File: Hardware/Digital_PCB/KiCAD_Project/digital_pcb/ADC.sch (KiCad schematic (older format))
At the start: 16 parts, among them U4 ADS1220, U5 KC2520B-C2

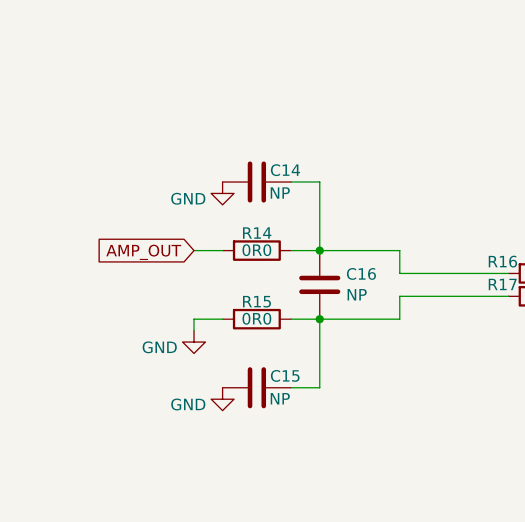
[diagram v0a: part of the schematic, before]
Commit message: Add pullups and divider for ADC input.
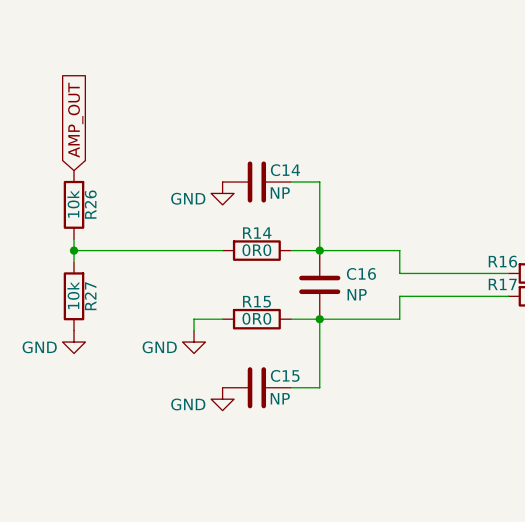
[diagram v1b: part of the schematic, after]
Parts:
- added R26, R27: 10k, Resistors_SMD:R_0603_HandSoldering, symbol Device:R
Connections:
- net AMP_OUT: now also R26.2; no longer R14.2
- net GND: now also R27.1
- new net: R14.2, R26.1, R27.2
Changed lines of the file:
@@
 Wire Wire Line
 	6150 3500 6150 3375
-Text GLabel 3525 2575 0    50   Input ~ 0
-AMP_OUT
-Wire Wire Line
-	3525 2575 3650 2575
 $Comp
 L power:GND #PWR032
@@
 NoConn ~ 5200 2975
 NoConn ~ 5200 3075
+Text GLabel 3000 2225 1    50   Input ~ 0
+AMP_OUT
+$Comp
+L Device:R R26
+U 1 1 5E0DD24D
+P 3000 2375
+F 0 "R26" V 2925 2375 50  0000 C CNN
+F 1 "10k" V 3000 2375 50  0000 C CNN
+F 2 "Resistors_SMD:R_0603_HandSoldering" V 2930 2375 50  0001 C CNN
+F 3 "~" H 3000 2375 50  0001 C CNN
+F 4 "1-0000010" H 3000 2375 50  0001 C CNN "Internal Part Number"
+F 5 "1" H 3000 2375 50  0001 C CNN "Populated"
+	1    3000 2375
+	-1   0    0    1
+$EndComp
+$Comp
+L Device:R R27
+U 1 1 5E0DD73A
+P 3000 2775
+F 0 "R27" V 2925 2775 50  0000 C CNN
+F 1 "10k" V 3000 2775 50  0000 C CNN
+F 2 "Resistors_SMD:R_0603_HandSoldering" V 2930 2775 50  0001 C CNN
+F 3 "~" H 3000 2775 50  0001 C CNN
+F 4 "1-0000010" H 3000 2775 50  0001 C CNN "Internal Part Number"
+F 5 "1" H 3000 2775 50  0001 C CNN "Populated"
+	1    3000 2775
+	-1   0    0    1
+$EndComp
+Wire Wire Line
+	3000 2525 3000 2575
+$Comp
+L power:GND #PWR082
+U 1 1 5E0DF9DE
+P 3000 2925
+F 0 "#PWR082" H 3000 2675 50  0001 C CNN
+F 1 "GND" H 2850 2850 50  0000 C CNN
+F 2 "" H 3000 2925 50  0001 C CNN
+F 3 "" H 3000 2925 50  0001 C CNN
+	1    3000 2925
+	1    0    0    -1
+$EndComp
+Connection ~ 3000 2575
+Wire Wire Line
+	3000 2575 3000 2625
+Wire Wire Line
+	3000 2575 3650 2575
 $EndSCHEMATC

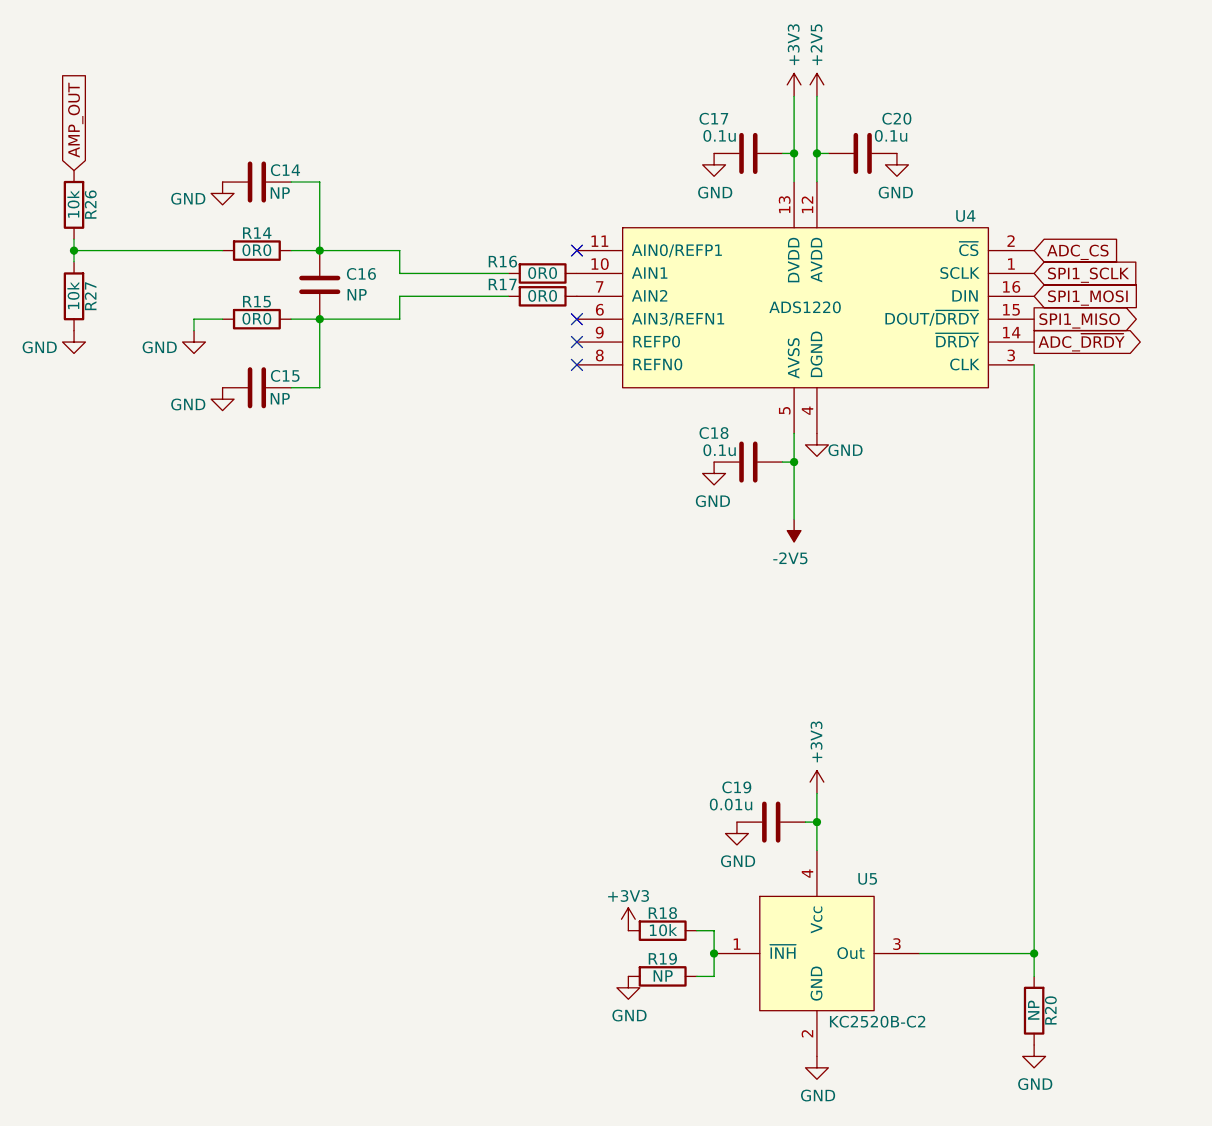
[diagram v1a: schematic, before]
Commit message: Digital PCB Rev 1.0 complete.
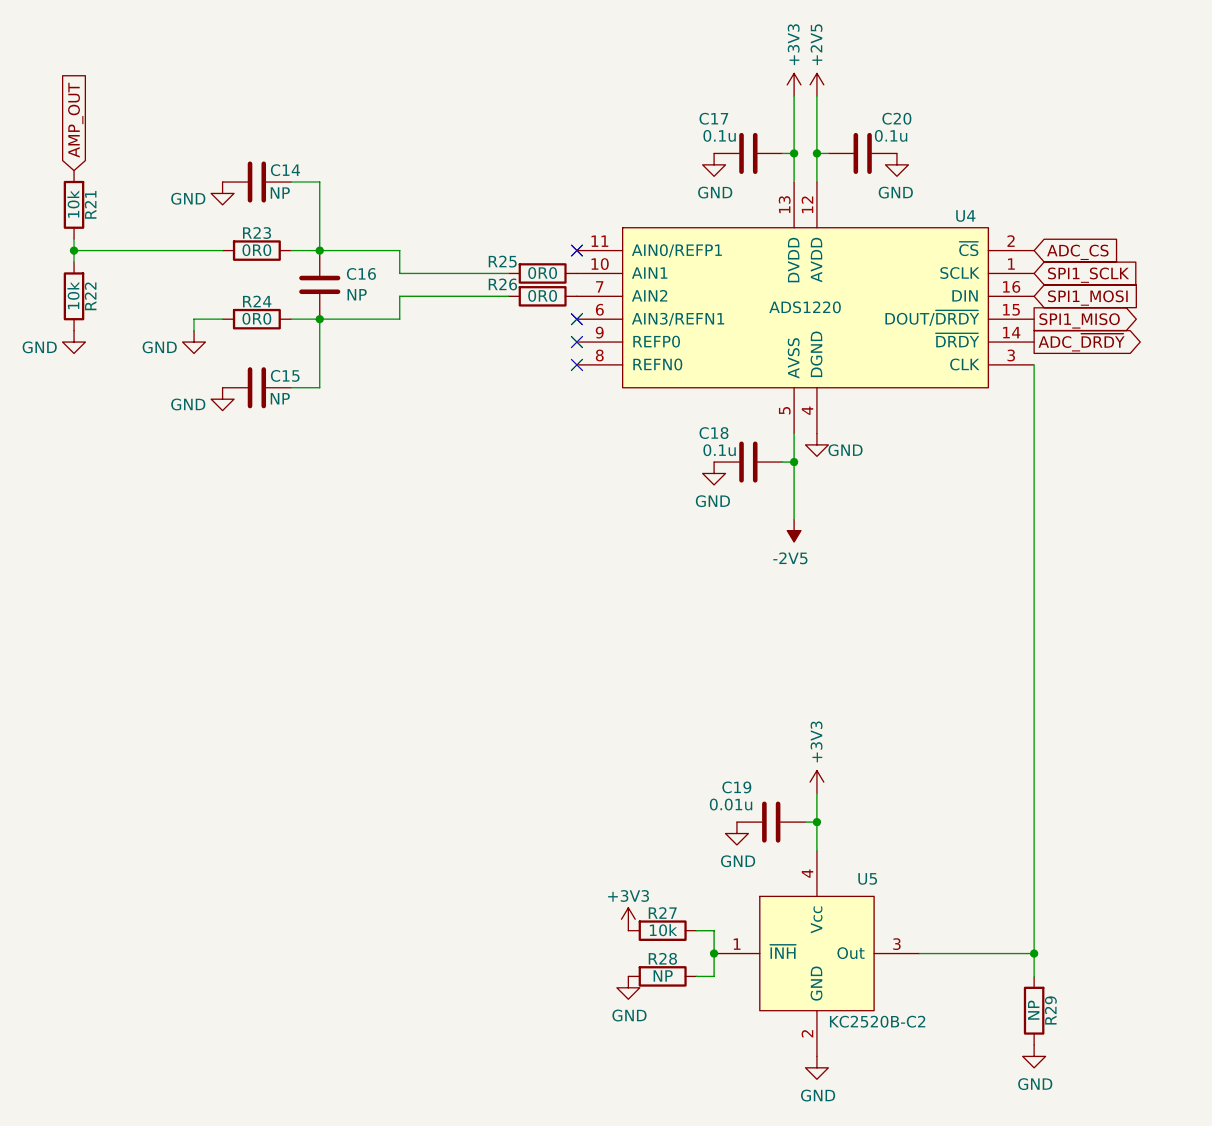
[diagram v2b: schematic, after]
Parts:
- renumbered R26 to R21, R27 to R22, R14 to R23, R15 to R24, R16 to R25, R17 to R26, R18 to R27, R19 to R28, R20 to R29
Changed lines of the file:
@@
 Sheet 3 5
 Title "Digital Rotating Electronics - NSSL EFM"
-Date "2019-11-26"
+Date "2019-12-30"
 Rev "1.0"
 Comp "Leeman Geophysical LLC"
@@
 $EndComp
 $Comp
-L Device:R R14
+L Device:R R23
 U 1 1 5DE0E4DD
 P 3800 2575
-F 0 "R14" V 3725 2575 50  0000 C CNN
+F 0 "R23" V 3725 2575 50  0000 C CNN
 F 1 "0R0" V 3800 2575 50  0000 C CNN
 F 2 "Resistors_SMD:R_0603_HandSoldering" V 3730 2575 50  0001 C CNN
@@
 $EndComp
 $Comp
-L Device:R R15
+L Device:R R24
 U 1 1 5DE0E9A7
 P 3800 2875
-F 0 "R15" V 3725 2875 50  0000 C CNN
+F 0 "R24" V 3725 2875 50  0000 C CNN
 F 1 "0R0" V 3800 2875 50  0000 C CNN
 F 2 "Resistors_SMD:R_0603_HandSoldering" V 3730 2875 50  0001 C CNN
@@
 $EndComp
 $Comp
-L power:GND #PWR034
+L power:GND #PWR044
 U 1 1 5DE1198C
 P 3650 3175
-F 0 "#PWR034" H 3650 2925 50  0001 C CNN
+F 0 "#PWR044" H 3650 2925 50  0001 C CNN
 F 1 "GND" H 3500 3100 50  0000 C CNN
 F 2 "" H 3650 3175 50  0001 C CNN
@@
 $EndComp
 $Comp
-L power:GND #PWR033
+L power:GND #PWR043
 U 1 1 5DE11F53
 P 3650 2275
-F 0 "#PWR033" H 3650 2025 50  0001 C CNN
+F 0 "#PWR043" H 3650 2025 50  0001 C CNN
 F 1 "GND" H 3500 2200 50  0000 C CNN
 F 2 "" H 3650 2275 50  0001 C CNN
@@
 Connection ~ 4075 2875
 $Comp
-L Device:R R16
+L Device:R R25
 U 1 1 5DE12E3C
 P 5050 2675
-F 0 "R16" V 5000 2500 50  0000 C CNN
+F 0 "R25" V 5000 2500 50  0000 C CNN
 F 1 "0R0" V 5050 2675 50  0000 C CNN
 F 2 "Resistors_SMD:R_0603_HandSoldering" V 4980 2675 50  0001 C CNN
@@
 $EndComp
 $Comp
-L Device:R R17
+L Device:R R26
 U 1 1 5DE1395D
 P 5050 2775
-F 0 "R17" V 5000 2600 50  0000 C CNN
+F 0 "R26" V 5000 2600 50  0000 C CNN
 F 1 "0R0" V 5050 2775 50  0000 C CNN
 F 2 "Resistors_SMD:R_0603_HandSoldering" V 4980 2775 50  0001 C CNN
@@
 	4425 2875 4075 2875
 $Comp
-L power:GND #PWR043
+L power:GND #PWR053
 U 1 1 5DE19D9A
 P 6250 3375
-F 0 "#PWR043" H 6250 3125 50  0001 C CNN
+F 0 "#PWR053" H 6250 3125 50  0001 C CNN
 F 1 "GND" H 6375 3300 50  0000 C CNN
 F 2 "" H 6250 3375 50  0001 C CNN
@@
 $EndComp
 $Comp
-L power:GND #PWR037
+L power:GND #PWR047
 U 1 1 5DE1BA91
 P 5800 2150
-F 0 "#PWR037" H 5800 1900 50  0001 C CNN
+F 0 "#PWR047" H 5800 1900 50  0001 C CNN
 F 1 "GND" H 5805 1977 50  0000 C CNN
 F 2 "" H 5800 2150 50  0001 C CNN
@@
 $EndComp
 $Comp
-L power:GND #PWR046
+L power:GND #PWR056
 U 1 1 5DE1D414
 P 6600 2150
-F 0 "#PWR046" H 6600 1900 50  0001 C CNN
+F 0 "#PWR056" H 6600 1900 50  0001 C CNN
 F 1 "GND" H 6605 1977 50  0000 C CNN
 F 2 "" H 6600 2150 50  0001 C CNN
@@
 $EndComp
 $Comp
-L power:+3V3 #PWR040
+L power:+3V3 #PWR050
 U 1 1 5DE1F225
 P 6150 1900
-F 0 "#PWR040" H 6150 1750 50  0001 C CNN
+F 0 "#PWR050" H 6150 1750 50  0001 C CNN
 F 1 "+3V3" V 6150 2125 50  0000 C CNN
 F 2 "" H 6150 1900 50  0001 C CNN
@@
 ADC_~DRDY
 $Comp
-L Device:R R20
+L Device:R R29
 U 1 1 5DE2F4F7
 P 7200 5900
-F 0 "R20" V 7125 5900 50  0000 C CNN
+F 0 "R29" V 7125 5900 50  0000 C CNN
 F 1 "NP" V 7200 5900 50  0000 C CNN
 F 2 "Resistors_SMD:R_0603_HandSoldering" V 7130 5900 50  0001 C CNN
@@
 $EndComp
 $Comp
-L power:GND #PWR045
+L power:GND #PWR055
 U 1 1 5DE30ACF
 P 6250 6100
-F 0 "#PWR045" H 6250 5850 50  0001 C CNN
+F 0 "#PWR055" H 6250 5850 50  0001 C CNN
 F 1 "GND" H 6255 5927 50  0000 C CNN
 F 2 "" H 6250 6100 50  0001 C CNN
@@
 $EndComp
 $Comp
-L power:GND #PWR039
+L power:GND #PWR049
 U 1 1 5DE33301
 P 5900 5075
-F 0 "#PWR039" H 5900 4825 50  0001 C CNN
+F 0 "#PWR049" H 5900 4825 50  0001 C CNN
 F 1 "GND" H 5905 4902 50  0000 C CNN
 F 2 "" H 5900 5075 50  0001 C CNN
@@
 $EndComp
 $Comp
-L power:+3V3 #PWR044
+L power:+3V3 #PWR054
 U 1 1 5DE33307
 P 6250 4950
-F 0 "#PWR044" H 6250 4800 50  0001 C CNN
+F 0 "#PWR054" H 6250 4800 50  0001 C CNN
 F 1 "+3V3" V 6250 5175 50  0000 C CNN
 F 2 "" H 6250 4950 50  0001 C CNN
@@
 Connection ~ 6250 5075
 $Comp
-L Device:R R19
+L Device:R R28
 U 1 1 5DE33F10
 P 5575 5750
-F 0 "R19" V 5500 5750 50  0000 C CNN
+F 0 "R28" V 5500 5750 50  0000 C CNN
 F 1 "NP" V 5575 5750 50  0000 C CNN
 F 2 "Resistors_SMD:R_0603_HandSoldering" V 5505 5750 50  0001 C CNN
@@
 $EndComp
 $Comp
-L Device:R R18
+L Device:R R27
 U 1 1 5DE3428C
 P 5575 5550
-F 0 "R18" V 5500 5550 50  0000 C CNN
+F 0 "R27" V 5500 5550 50  0000 C CNN
 F 1 "10k" V 5575 5550 50  0000 C CNN
 F 2 "Resistors_SMD:R_0603_HandSoldering" V 5505 5550 50  0001 C CNN
@@
 Connection ~ 5800 5650
 $Comp
-L power:+3V3 #PWR035
+L power:+3V3 #PWR045
 U 1 1 5DE35C3C
 P 5425 5550
-F 0 "#PWR035" H 5425 5400 50  0001 C CNN
+F 0 "#PWR045" H 5425 5400 50  0001 C CNN
 F 1 "+3V3" H 5425 5700 50  0000 C CNN
 F 2 "" H 5425 5550 50  0001 C CNN
@@
 $EndComp
 $Comp
-L power:GND #PWR036
+L power:GND #PWR046
 U 1 1 5DE3628A
 P 5425 5750
-F 0 "#PWR036" H 5425 5500 50  0001 C CNN
+F 0 "#PWR046" H 5425 5500 50  0001 C CNN
 F 1 "GND" H 5430 5577 50  0000 C CNN
 F 2 "" H 5425 5750 50  0001 C CNN
@@
 Connection ~ 7200 5650
 $Comp
-L power:GND #PWR047
+L power:GND #PWR057
 U 1 1 5DE3C406
 P 7200 6050
-F 0 "#PWR047" H 7200 5800 50  0001 C CNN
+F 0 "#PWR057" H 7200 5800 50  0001 C CNN
 F 1 "GND" H 7205 5877 50  0000 C CNN
 F 2 "" H 7200 6050 50  0001 C CNN
@@
 P 6150 3750
 AR Path="/5DE673A0/5E0DC879" Ref="#PWR?"  Part="1"
-AR Path="/5DE0D3F3/5E0DC879" Ref="#PWR041"  Part="1"
-F 0 "#PWR041" H 6150 3850 50  0001 C CNN
+AR Path="/5DE0D3F3/5E0DC879" Ref="#PWR051"  Part="1"
+F 0 "#PWR051" H 6150 3850 50  0001 C CNN
 F 1 "-2V5" H 6165 3923 50  0000 C CNN
 F 2 "" H 6150 3750 50  0001 C CNN
@@
 P 6250 1900
 AR Path="/5DE673A0/5E0DC87F" Ref="#PWR?"  Part="1"
-AR Path="/5DE0D3F3/5E0DC87F" Ref="#PWR042"  Part="1"
-F 0 "#PWR042" H 6250 1750 50  0001 C CNN
+AR Path="/5DE0D3F3/5E0DC87F" Ref="#PWR052"  Part="1"
+F 0 "#PWR052" H 6250 1750 50  0001 C CNN
 F 1 "+2V5" V 6250 2125 50  0000 C CNN
 F 2 "" H 6250 1900 50  0001 C CNN
@@
 $EndComp
 $Comp
-L power:GND #PWR038
+L power:GND #PWR048
 U 1 1 5E0DE063
 P 5800 3500
-F 0 "#PWR038" H 5800 3250 50  0001 C CNN
+F 0 "#PWR048" H 5800 3250 50  0001 C CNN
 F 1 "GND" H 5805 3327 50  0000 C CNN
 F 2 "" H 5800 3500 50  0001 C CNN
@@
 	6150 3500 6150 3375
 $Comp
-L power:GND #PWR032
+L power:GND #PWR042
 U 1 1 5E0FF166
 P 3525 2925
-F 0 "#PWR032" H 3525 2675 50  0001 C CNN
+F 0 "#PWR042" H 3525 2675 50  0001 C CNN
 F 1 "GND" H 3375 2850 50  0000 C CNN
 F 2 "" H 3525 2925 50  0001 C CNN
@@
 AMP_OUT
 $Comp
-L Device:R R26
+L Device:R R21
 U 1 1 5E0DD24D
 P 3000 2375
-F 0 "R26" V 2925 2375 50  0000 C CNN
+F 0 "R21" V 2925 2375 50  0000 C CNN
 F 1 "10k" V 3000 2375 50  0000 C CNN
 F 2 "Resistors_SMD:R_0603_HandSoldering" V 2930 2375 50  0001 C CNN
@@
 $EndComp
 $Comp
-L Device:R R27
+L Device:R R22
 U 1 1 5E0DD73A
 P 3000 2775
-F 0 "R27" V 2925 2775 50  0000 C CNN
+F 0 "R22" V 2925 2775 50  0000 C CNN
 F 1 "10k" V 3000 2775 50  0000 C CNN
 F 2 "Resistors_SMD:R_0603_HandSoldering" V 2930 2775 50  0001 C CNN
@@
 	3000 2525 3000 2575
 $Comp
-L power:GND #PWR082
+L power:GND #PWR041
 U 1 1 5E0DF9DE
 P 3000 2925
-F 0 "#PWR082" H 3000 2675 50  0001 C CNN
+F 0 "#PWR041" H 3000 2675 50  0001 C CNN
 F 1 "GND" H 2850 2850 50  0000 C CNN
 F 2 "" H 3000 2925 50  0001 C CNN
